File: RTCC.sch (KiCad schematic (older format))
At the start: 5 parts

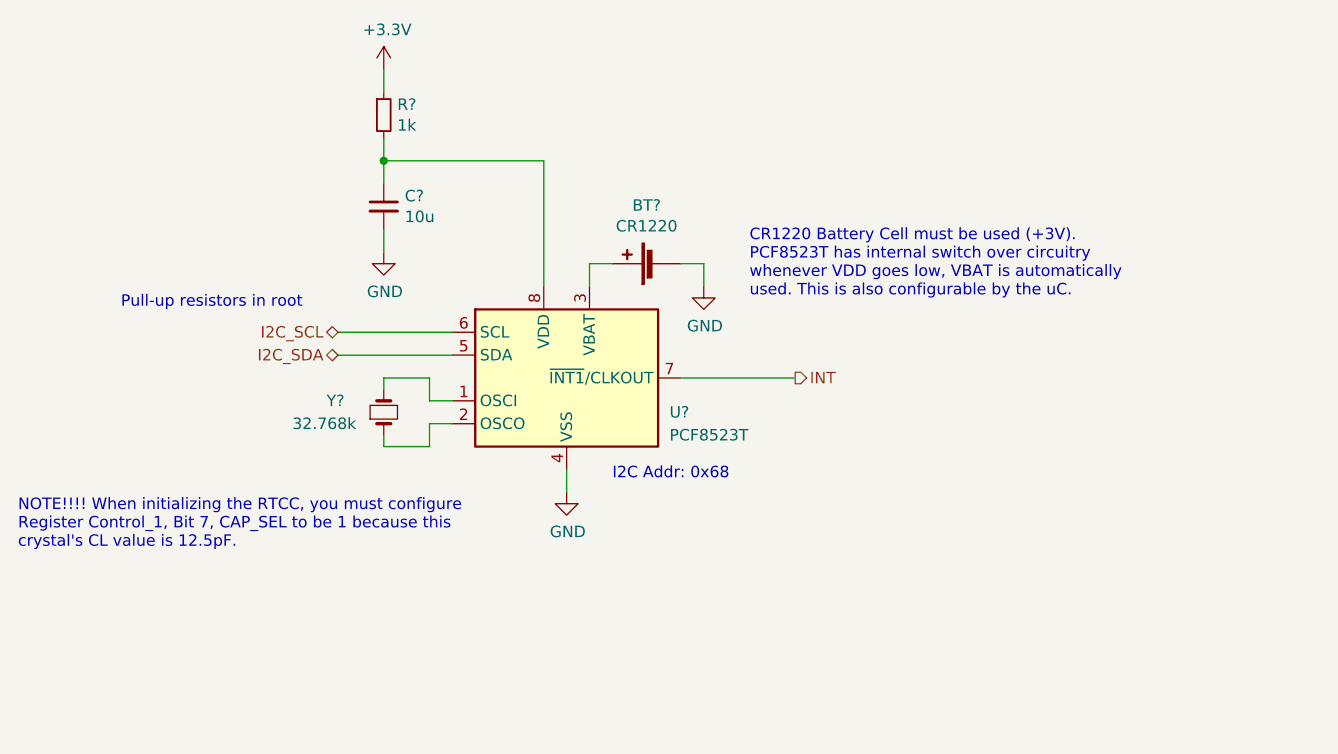
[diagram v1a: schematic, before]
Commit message: Adds logic analyzer points and LEDs
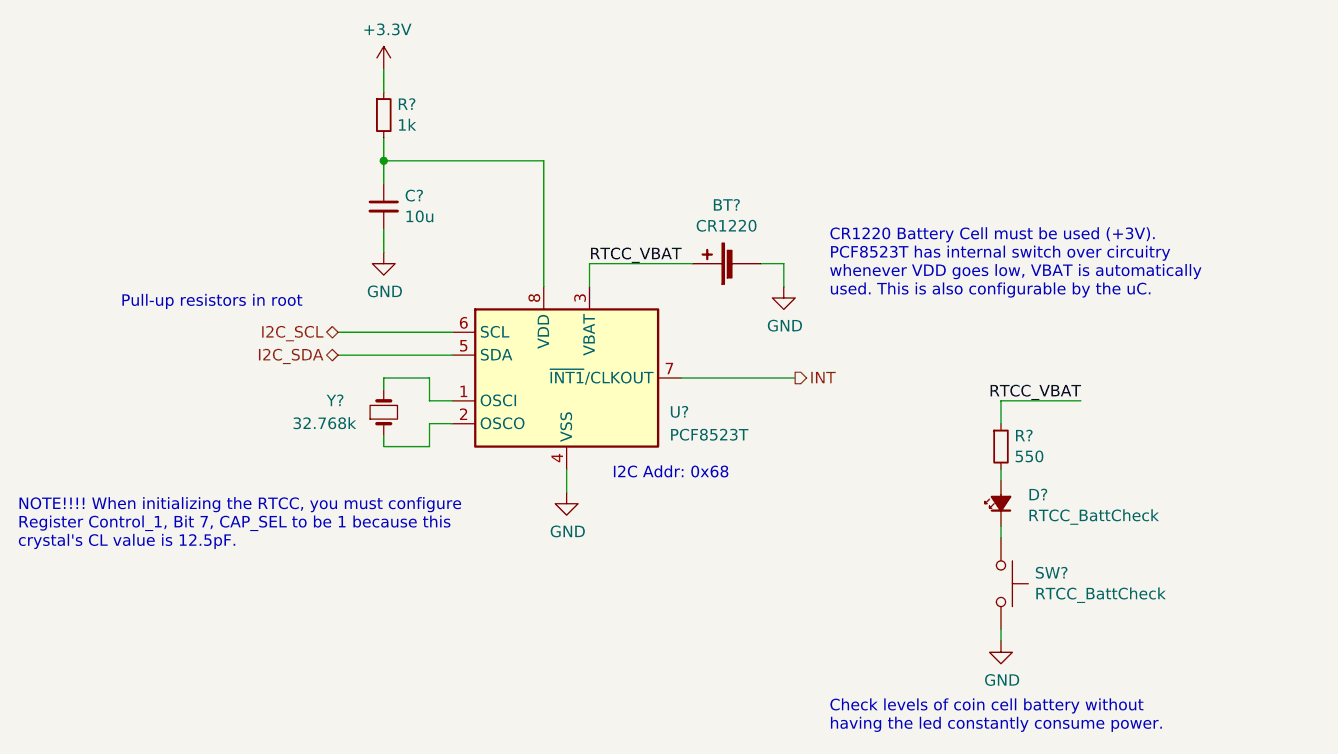
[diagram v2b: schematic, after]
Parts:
- added D?: RTCC_BattCheck, LED_SMD:LED_0805_2012Metric, symbol Device:LED_Small_ALT
- added R?: 550, Resistor_SMD:R_0805_2012Metric, symbol Device:R_Small
- added SW?: RTCC_BattCheck, Button_Switch_SMD:SW_SPST_B3SL-1002P, symbol Switch:SW_Push
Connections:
- net GND: now also SW?.2
- net RTCC_VBAT: now reaches BT?.1 (+), U?.3 (VBAT)
- net RTCC_VBAT: now also R?.1
- new net: D?.1 (K), SW?.1
- new net: D?.2 (A), R?.2
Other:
- note added: "Check levels of coin cell battery without\nhaving the led constantly consume power."
- moved on the sheet: BT?
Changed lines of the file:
@@
 L Device:Battery_Cell BT?
 U 1 1 5F6F3DAC
-P 5400 3250
-F 0 "BT?" V 5655 3300 50  0000 C CNN
-F 1 "CR1220" V 5564 3300 50  0000 C CNN
-F 2 "Battery:BatteryHolder_Keystone_3000_1x12mm" V 5400 3310 50  0001 C CNN
-F 3 "~" V 5400 3310 50  0001 C CNN
-	1    5400 3250
+P 5750 3250
+F 0 "BT?" V 6005 3300 50  0000 C CNN
+F 1 "CR1220" V 5914 3300 50  0000 C CNN
+F 2 "Battery:BatteryHolder_Keystone_3000_1x12mm" V 5750 3310 50  0001 C CNN
+F 3 "~" V 5750 3310 50  0001 C CNN
+	1    5750 3250
 	0    -1   -1   0
 $EndComp
 Wire Wire Line
 	5100 3350 5100 3250
-Wire Wire Line
-	5100 3250 5200 3250
 $Comp
 L power:GND #PWR?
 U 1 1 5F6F5C5D
-P 5600 3350
-F 0 "#PWR?" H 5600 3100 50  0001 C CNN
-F 1 "GND" H 5605 3177 50  0000 C CNN
-F 2 "" H 5600 3350 50  0001 C CNN
-F 3 "" H 5600 3350 50  0001 C CNN
-	1    5600 3350
-	1    0    0    -1
-$EndComp
-Wire Wire Line
-	5600 3350 5600 3250
-Wire Wire Line
-	5600 3250 5500 3250
+P 5950 3350
+F 0 "#PWR?" H 5950 3100 50  0001 C CNN
+F 1 "GND" H 5955 3177 50  0000 C CNN
+F 2 "" H 5950 3350 50  0001 C CNN
+F 3 "" H 5950 3350 50  0001 C CNN
+	1    5950 3350
+	1    0    0    -1
+$EndComp
+Wire Wire Line
+	5950 3350 5950 3250
+Wire Wire Line
+	5950 3250 5850 3250
 $Comp
 L Device:R_Small R?
@@
 	1    0    0    -1
 $EndComp
-Text Notes 5800 3400 0    50   ~ 0
+Text Notes 6150 3400 0    50   ~ 0
 CR1220 Battery Cell must be used (+3V).\nPCF8523T has internal switch over circuitry\nwhenever VDD goes low, VBAT is automatically\nused. This is also configurable by the uC.
 $Comp
@@
 Wire Wire Line
 	6000 3750 5500 3750
+$Comp
+L power:GND #PWR?
+U 1 1 5FD2F1FE
+P 6900 4900
+AR Path="/5F6CDFD6/5FD2F1FE" Ref="#PWR?"  Part="1"
+AR Path="/5F6EFD51/5FD2F1FE" Ref="#PWR?"  Part="1"
+AR Path="/5F6F1E63/5FD2F1FE" Ref="#PWR?"  Part="1"
+F 0 "#PWR?" H 6900 4650 50  0001 C CNN
+F 1 "GND" H 6905 4727 50  0000 C CNN
+F 2 "" H 6900 4900 50  0001 C CNN
+F 3 "" H 6900 4900 50  0001 C CNN
+	1    6900 4900
+	1    0    0    -1
+$EndComp
+$Comp
+L Device:LED_Small_ALT D?
+U 1 1 5FD2F208
+P 6900 4300
+AR Path="/5F6CDFD6/5FD2F208" Ref="D?"  Part="1"
+AR Path="/5F6EFD51/5FD2F208" Ref="D?"  Part="1"
+AR Path="/5F6F1E63/5FD2F208" Ref="D?"  Part="1"
+F 0 "D?" V 6938 4182 50  0000 R CNN
+F 1 "RTCC_BattCheck" V 6847 4182 50  0000 R CNN
+F 2 "LED_SMD:LED_0805_2012Metric" H 6900 4300 50  0001 C CNN
+F 3 "~" H 6900 4300 50  0001 C CNN
+F 4 "Green" V 6900 4300 50  0001 C CNN "Color"
+F 5 "APTD2012LCGCK" V 6900 4300 50  0001 C CNN "P/N"
+F 6 "1.9V" V 6900 4300 50  0001 C CNN "Vf"
+F 7 "2mA" V 6900 4300 50  0001 C CNN "If"
+	1    6900 4300
+	0    -1   -1   0
+$EndComp
+Wire Wire Line
+	6900 4450 6900 4400
+Wire Wire Line
+	6900 3850 6900 3950
+Wire Wire Line
+	7250 3850 6900 3850
+$Comp
+L Device:R_Small R?
+U 1 1 5FD2F211
+P 6900 4050
+AR Path="/5F6EFD51/5FD2F211" Ref="R?"  Part="1"
+AR Path="/5F6F1E63/5FD2F211" Ref="R?"  Part="1"
+F 0 "R?" H 6959 4096 50  0000 L CNN
+F 1 "550" H 6959 4005 50  0000 L CNN
+F 2 "Resistor_SMD:R_0805_2012Metric" H 6900 4050 50  0001 C CNN
+F 3 "~" H 6900 4050 50  0001 C CNN
+	1    6900 4050
+	1    0    0    -1
+$EndComp
+Wire Wire Line
+	6900 4200 6900 4150
+Wire Wire Line
+	6900 4850 6900 4900
+Text Notes 6150 5300 0    50   ~ 0
+Check levels of coin cell battery without\nhaving the led constantly consume power.
+Text Label 5100 3250 0    50   ~ 0
+RTCC_VBAT
+Wire Wire Line
+	5100 3250 5550 3250
+Text Label 7250 3850 2    50   ~ 0
+RTCC_VBAT
+$Comp
+L Switch:SW_Push SW?
+U 1 1 5FD3AF49
+P 6900 4650
+AR Path="/5FD3AF49" Ref="SW?"  Part="1"
+AR Path="/5F6F1E63/5FD3AF49" Ref="SW?"  Part="1"
+F 0 "SW?" V 6854 4798 50  0000 L CNN
+F 1 "RTCC_BattCheck" V 6945 4798 50  0000 L CNN
+F 2 "Button_Switch_SMD:SW_SPST_B3SL-1002P" H 6900 4850 50  0001 C CNN
+F 3 "~" H 6900 4850 50  0001 C CNN
+F 4 "EVQ-7Q203W or B3SL-1002P" V 6900 4650 50  0001 C CNN "P/N"
+	1    6900 4650
+	0    1    1    0
+$EndComp
 $EndSCHEMATC

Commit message: Initial layout of the Telemtry board.
The ethernet interface needs more work.
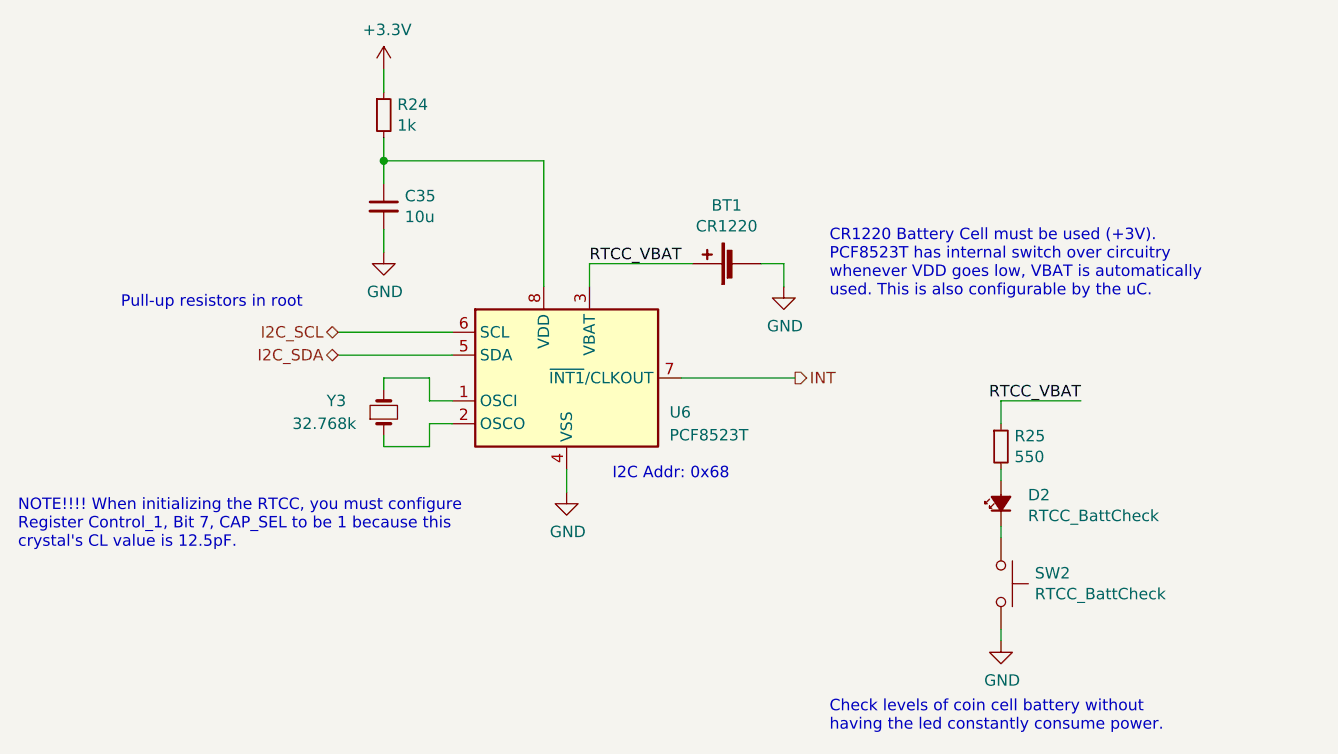
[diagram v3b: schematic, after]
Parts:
- gave numbers to parts that had none: 8
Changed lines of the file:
@@
 $EndDescr
 $Comp
-L Timer_RTC:PCF8523T U?
+L Timer_RTC:PCF8523T U6
 U 1 1 5F6F240B
 P 5000 3750
-F 0 "U?" H 5450 3600 50  0000 L CNN
+F 0 "U6" H 5450 3600 50  0000 L CNN
 F 1 "PCF8523T" H 5450 3500 50  0000 L CNN
 F 2 "Package_SO:SOIC-8_3.9x4.9mm_P1.27mm" H 5800 3400 50  0001 C CNN
@@
 	4000 3650 4500 3650
 $Comp
-L Device:Battery_Cell BT?
+L Device:Battery_Cell BT1
 U 1 1 5F6F3DAC
 P 5750 3250
-F 0 "BT?" V 6005 3300 50  0000 C CNN
+F 0 "BT1" V 6005 3300 50  0000 C CNN
 F 1 "CR1220" V 5914 3300 50  0000 C CNN
 F 2 "Battery:BatteryHolder_Keystone_3000_1x12mm" V 5750 3310 50  0001 C CNN
@@
 	5100 3350 5100 3250
 $Comp
-L power:GND #PWR?
+L power:GND #PWR0149
 U 1 1 5F6F5C5D
 P 5950 3350
-F 0 "#PWR?" H 5950 3100 50  0001 C CNN
+F 0 "#PWR0149" H 5950 3100 50  0001 C CNN
 F 1 "GND" H 5955 3177 50  0000 C CNN
 F 2 "" H 5950 3350 50  0001 C CNN
@@
 	5950 3250 5850 3250
 $Comp
-L Device:R_Small R?
+L Device:R_Small R24
 U 1 1 5F6F70B9
 P 4200 2600
-F 0 "R?" H 4259 2646 50  0000 L CNN
+F 0 "R24" H 4259 2646 50  0000 L CNN
 F 1 "1k" H 4259 2555 50  0000 L CNN
 F 2 "Resistor_SMD:R_0805_2012Metric" V 4130 2600 50  0001 C CNN
@@
 CR1220 Battery Cell must be used (+3V).\nPCF8523T has internal switch over circuitry\nwhenever VDD goes low, VBAT is automatically\nused. This is also configurable by the uC.
 $Comp
-L Device:C_Small C?
+L Device:C_Small C35
 U 1 1 5F6F8378
 P 4200 3000
-F 0 "C?" H 4292 3046 50  0000 L CNN
+F 0 "C35" H 4292 3046 50  0000 L CNN
 F 1 "10u" H 4292 2955 50  0000 L CNN
 F 2 "Capacitor_SMD:C_0805_2012Metric" H 4238 2850 50  0001 C CNN
@@
 I2C Addr: 0x68
 $Comp
-L power:+3.3V #PWR?
+L power:+3.3V #PWR0150
 U 1 1 5F702584
 P 4200 2400
-F 0 "#PWR?" H 4200 2250 50  0001 C CNN
+F 0 "#PWR0150" H 4200 2250 50  0001 C CNN
 F 1 "+3.3V" H 4215 2573 50  0000 C CNN
 F 2 "" H 4200 2400 50  0001 C CNN
@@
 $EndComp
 $Comp
-L power:GND #PWR?
+L power:GND #PWR0151
 U 1 1 5F702D22
 P 4200 3200
-F 0 "#PWR?" H 4200 2950 50  0001 C CNN
+F 0 "#PWR0151" H 4200 2950 50  0001 C CNN
 F 1 "GND" H 4205 3027 50  0000 C CNN
 F 2 "" H 4200 3200 50  0001 C CNN
@@
 	4200 2800 4200 2900
 $Comp
-L Device:Crystal_Small Y?
+L Device:Crystal_Small Y3
 U 1 1 5F704FF5
 P 4200 3900
-F 0 "Y?" V 4250 3650 50  0000 L CNN
+F 0 "Y3" V 4250 3650 50  0000 L CNN
 F 1 "32.768k" V 4150 3500 50  0000 L CNN
 F 2 "Crystal:Crystal_SMD_Abracon_ABS25-4Pin_8.0x3.8mm" H 4200 3900 50  0001 C CNN
@@
 NOTE!!!! When initializing the RTCC, you must configure\nRegister Control_1, Bit 7, CAP_SEL to be 1 because this\ncrystal's CL value is 12.5pF.
 $Comp
-L power:GND #PWR?
+L power:GND #PWR0152
 U 1 1 5F709C37
 P 5000 4250
-F 0 "#PWR?" H 5000 4000 50  0001 C CNN
+F 0 "#PWR0152" H 5000 4000 50  0001 C CNN
 F 1 "GND" H 5005 4077 50  0000 C CNN
 F 2 "" H 5000 4250 50  0001 C CNN
@@
 AR Path="/5F6CDFD6/5FD2F1FE" Ref="#PWR?"  Part="1"
 AR Path="/5F6EFD51/5FD2F1FE" Ref="#PWR?"  Part="1"
-AR Path="/5F6F1E63/5FD2F1FE" Ref="#PWR?"  Part="1"
-F 0 "#PWR?" H 6900 4650 50  0001 C CNN
+AR Path="/5F6F1E63/5FD2F1FE" Ref="#PWR0153"  Part="1"
+F 0 "#PWR0153" H 6900 4650 50  0001 C CNN
 F 1 "GND" H 6905 4727 50  0000 C CNN
 F 2 "" H 6900 4900 50  0001 C CNN
@@
 AR Path="/5F6CDFD6/5FD2F208" Ref="D?"  Part="1"
 AR Path="/5F6EFD51/5FD2F208" Ref="D?"  Part="1"
-AR Path="/5F6F1E63/5FD2F208" Ref="D?"  Part="1"
-F 0 "D?" V 6938 4182 50  0000 R CNN
+AR Path="/5F6F1E63/5FD2F208" Ref="D2"  Part="1"
+F 0 "D2" V 6938 4182 50  0000 R CNN
 F 1 "RTCC_BattCheck" V 6847 4182 50  0000 R CNN
 F 2 "LED_SMD:LED_0805_2012Metric" H 6900 4300 50  0001 C CNN
@@
 P 6900 4050
 AR Path="/5F6EFD51/5FD2F211" Ref="R?"  Part="1"
-AR Path="/5F6F1E63/5FD2F211" Ref="R?"  Part="1"
-F 0 "R?" H 6959 4096 50  0000 L CNN
+AR Path="/5F6F1E63/5FD2F211" Ref="R25"  Part="1"
+F 0 "R25" H 6959 4096 50  0000 L CNN
 F 1 "550" H 6959 4005 50  0000 L CNN
 F 2 "Resistor_SMD:R_0805_2012Metric" H 6900 4050 50  0001 C CNN
@@
 P 6900 4650
 AR Path="/5FD3AF49" Ref="SW?"  Part="1"
-AR Path="/5F6F1E63/5FD3AF49" Ref="SW?"  Part="1"
-F 0 "SW?" V 6854 4798 50  0000 L CNN
+AR Path="/5F6F1E63/5FD3AF49" Ref="SW2"  Part="1"
+F 0 "SW2" V 6854 4798 50  0000 L CNN
 F 1 "RTCC_BattCheck" V 6945 4798 50  0000 L CNN
 F 2 "Button_Switch_SMD:SW_SPST_B3SL-1002P" H 6900 4850 50  0001 C CNN

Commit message: Lay out the Telemetry board.
This is the initial draft of the Telemetry board layout. A few
debugging pins changed (on the SD card) for easier routing.

There is still some uncertainty with regard to the routing of the
Ethernet traces. According to my calculations, the differential
impedence between the RX+/- traces and the TX+/- traces is around
150R, which is 50% higher than one source was recommending. I am
uncertain how to reduce this though, and I am unclear as to how
much this will affect performance, especially when the traces
cover such a short distance.
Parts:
- U6: symbol Timer_RTC:PCF8523T -> Telemetry-Primary-rescue:PCF8523T-Timer_RTC
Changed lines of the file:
@@
 $EndDescr
 $Comp
-L Timer_RTC:PCF8523T U6
+L Telemetry-Primary-rescue:PCF8523T-Timer_RTC U6
 U 1 1 5F6F240B
 P 5000 3750
